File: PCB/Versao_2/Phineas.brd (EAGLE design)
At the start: 160 x 100 mm, 11 parts

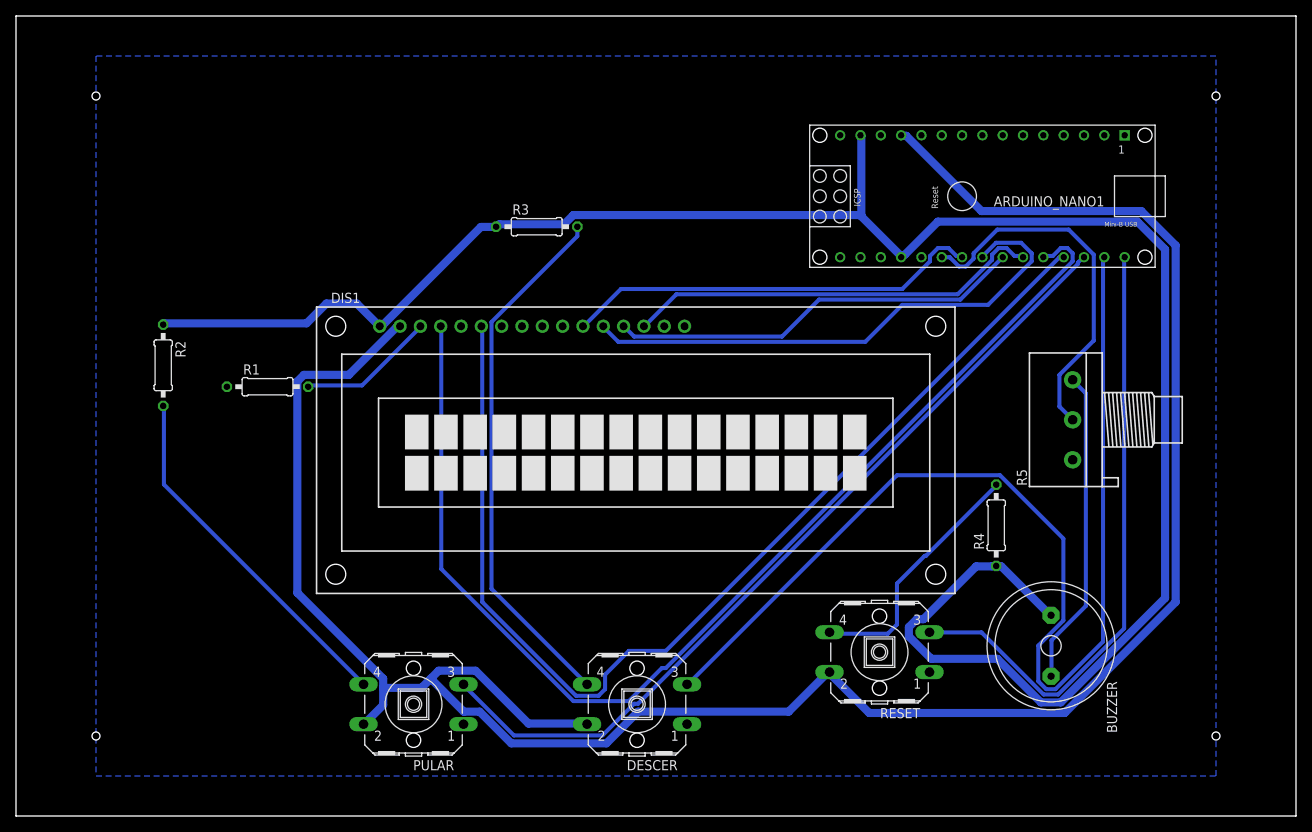
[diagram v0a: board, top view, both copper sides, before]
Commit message: Alterando esquemático e board Phineas
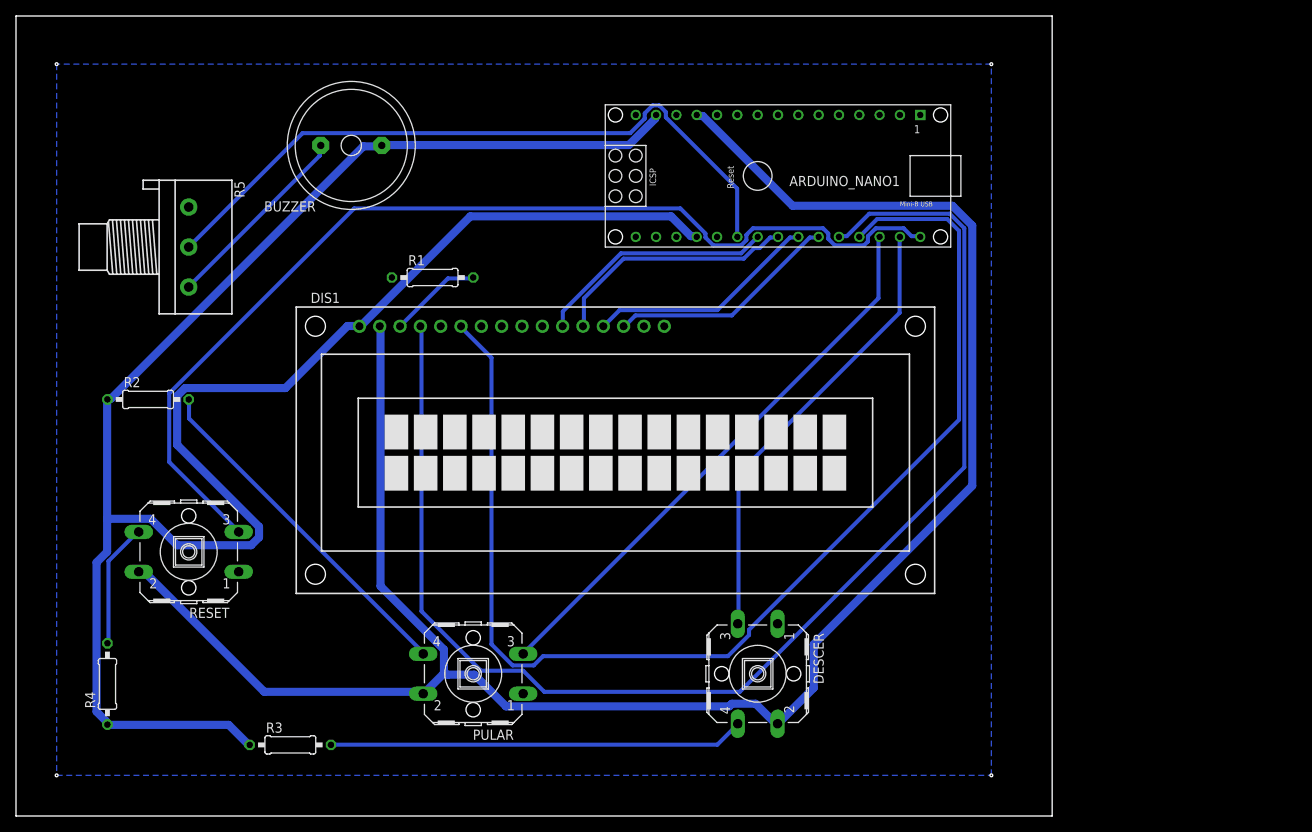
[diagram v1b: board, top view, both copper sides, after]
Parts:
- moved R4 112.9 mm to (11.4, 16.5)
- moved R5 112.6 mm to (21.6, 71.1), turned to 270 degrees
- moved BUZZER 107.5 mm to (41.9, 83.8), turned to 180 degrees
- moved RESET 87.3 mm to (21.6, 33.0)
- moved R3 71.7 mm to (34.3, 8.89)
- moved ARDUINO_NANO1 25.7 mm to (92.7, 80.0)
- moved R1 24.7 mm to (52.1, 67.3)
- moved DESCER 15.6 mm to (92.7, 17.8), turned to 270 degrees
- moved PULAR 8.38 mm to (57.1, 17.8)
- moved R2 4.67 mm to (16.5, 52.1), turned to 0 degrees
- moved DIS1 2.54 mm to (74.9, 45.7)
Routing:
- net N$7: track 139.4 -> 56.8 mm
- net N$6: track 77.4 -> 130.8 mm
- net N$18: track 46.2 -> 87.0 mm
- net VCC: track 285.8 -> 249.3 mm
- net N$13: track 67.1 -> 31.0 mm
- net N$8: track 105.1 -> 70.6 mm
- net N$11: track 52.3 -> 29.0 mm
- net N$12: track 52.0 -> 29.0 mm
- net N$5: track 144.4 -> 166.8 mm
- net N$14: track 52.3 -> 30.1 mm
- net N$15: track 31.7 -> 15.7 mm
- net N$9: track 135.8 -> 151.6 mm
- net N$10: track 39.6 -> 24.5 mm
- net N$4: track 66.6 -> 52.0 mm
- net N$2: track 17.2 -> 11.7 mm
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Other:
- board size 160 x 100 mm -> 129.5 x 100 mm
